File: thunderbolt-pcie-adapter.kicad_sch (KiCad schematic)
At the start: 8 parts

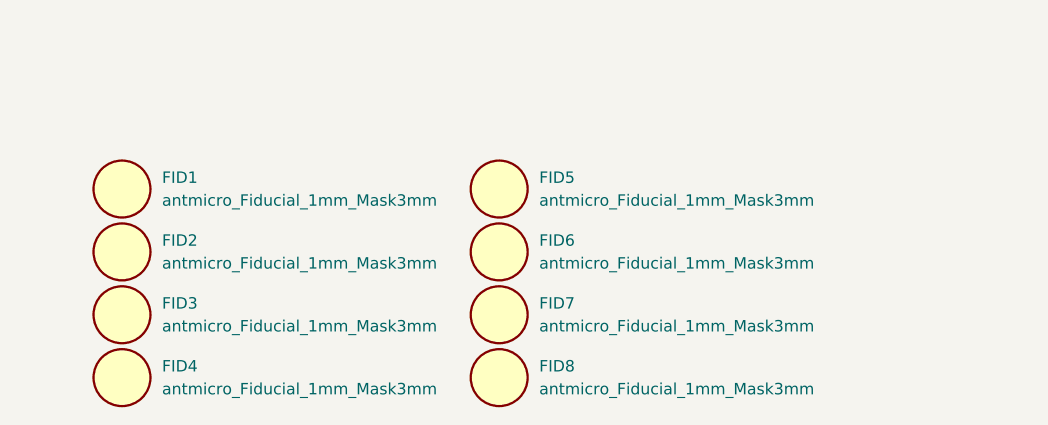
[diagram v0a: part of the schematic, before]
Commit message: Introduce component standardization
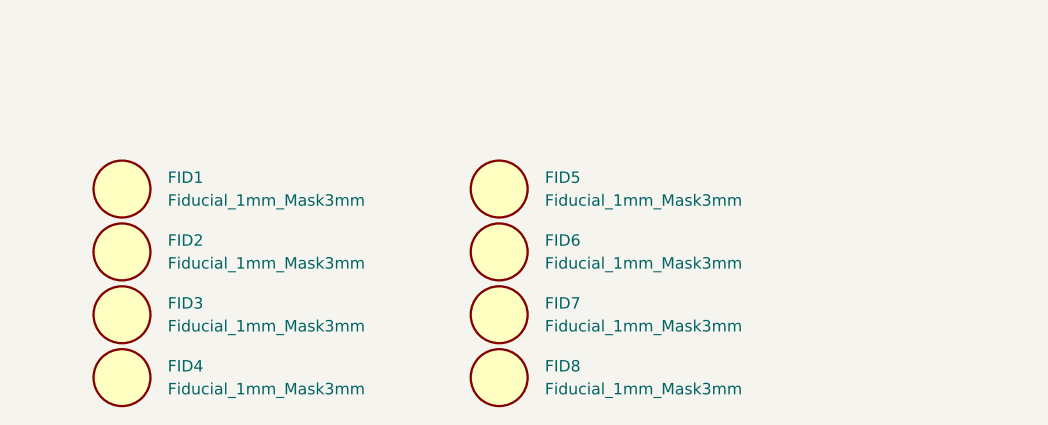
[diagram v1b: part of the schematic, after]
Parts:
- FID1, FID2, FID3, FID4, FID5, FID6, FID7, FID8: value antmicro_Fiducial_1mm_Mask3mm -> Fiducial_1mm_Mask3mm; symbol thunderbolt-pcie-adapter:antmicro_Fiducial_1mm_Mask3mm -> thunderbolt-pcie-adapter:Fiducial_1mm_Mask3mm
